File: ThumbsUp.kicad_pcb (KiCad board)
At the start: 2 copper layers, 215.3 x 226 mm, 51 parts, among them J1 52559-1233, J10 Raiser_Male, J13 Raiser_Female, J14 Raiser_Male, J19 Raiser_Female, J1L1 PJ-3200B, J1R1 PJ-3200B, J2 52559-1233, J33 Raiser_Male, J34 Raiser_Female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

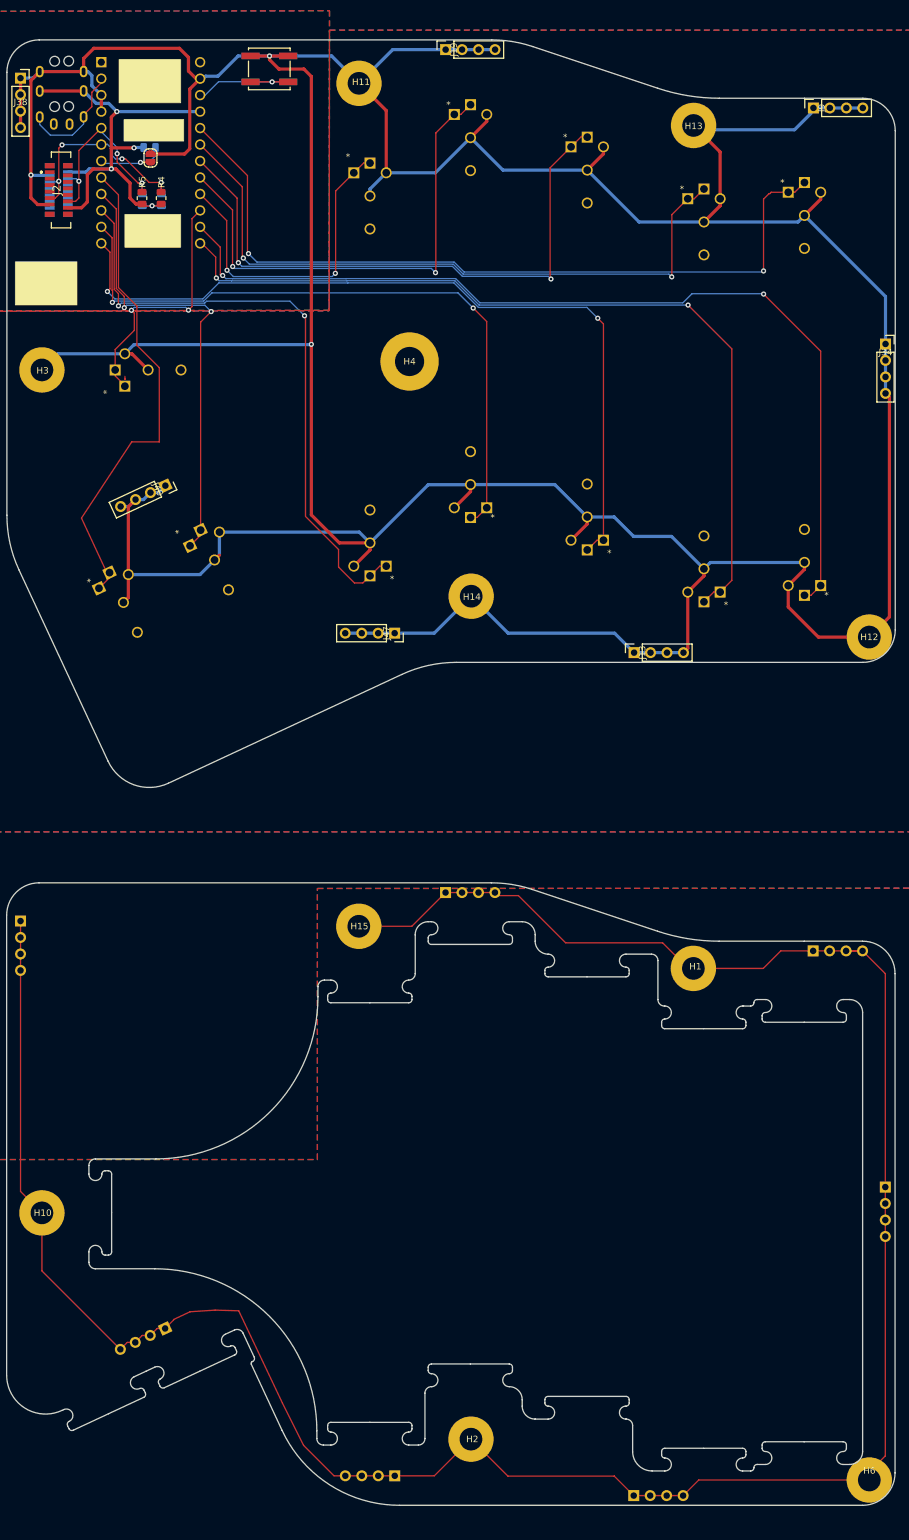
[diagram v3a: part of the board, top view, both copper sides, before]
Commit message: K12: Moved the top border a bit to thicken the bridge between -L and -T. Shuffled the stand-offs and headers around to space them more evenly.//TODO: generate Gerbers
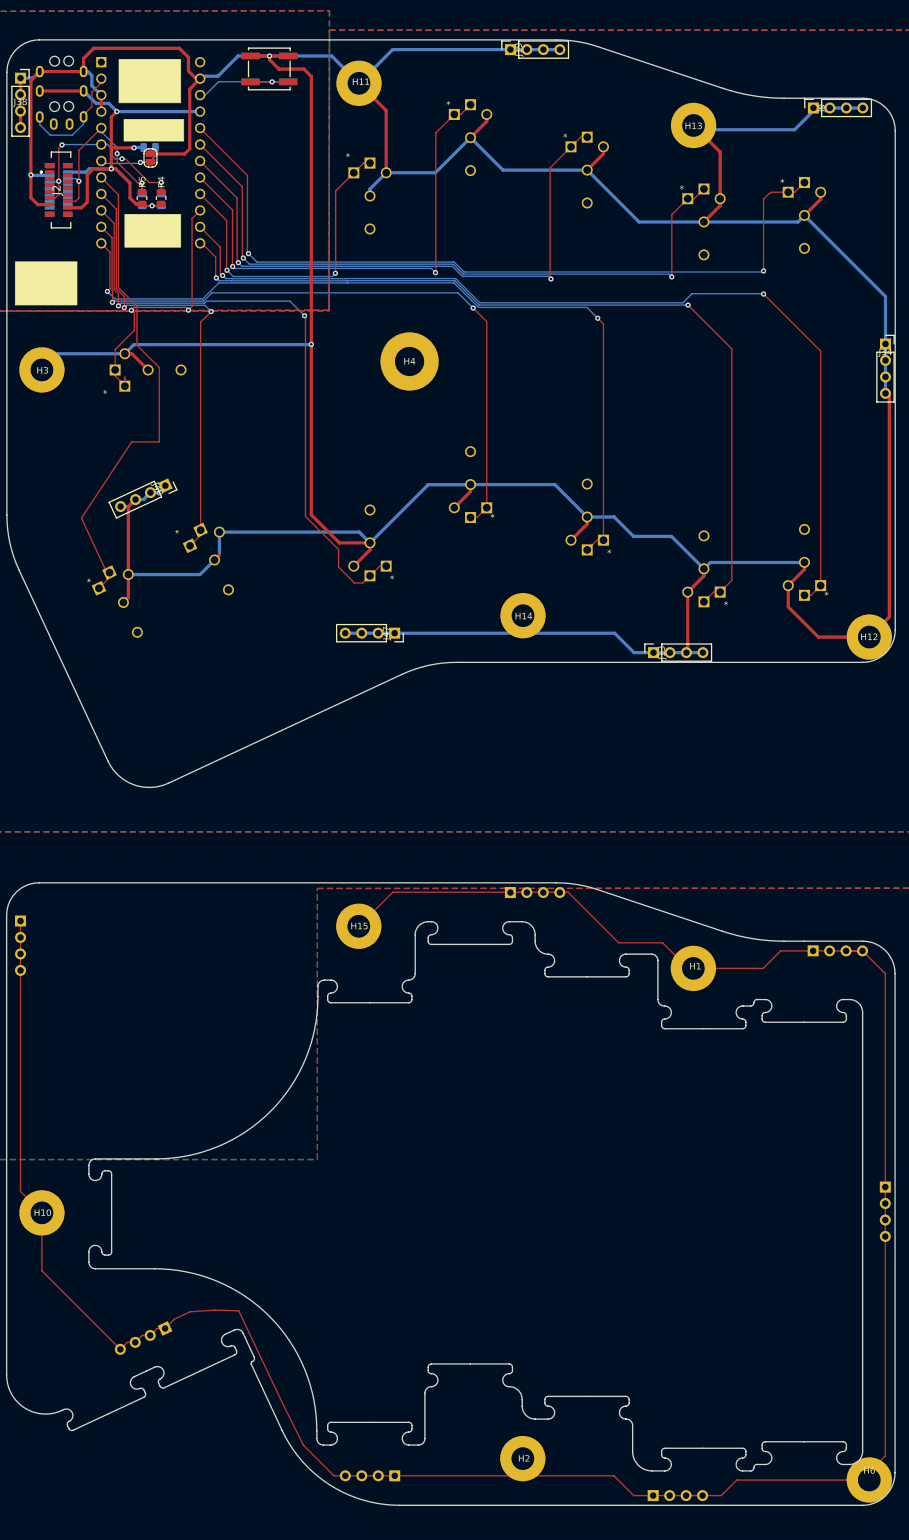
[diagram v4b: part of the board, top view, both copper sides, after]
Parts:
- moved J19 10.0 mm to (109.2, 27.0)
- moved J33 10.0 mm to (109.1, 157.0)
- moved H14 8.54 mm to (111.1, 114.3)
- moved H2 8.54 mm to (111.1, 244.3)
- moved J13 3.00 mm to (131.2, 120.0)
- moved J14 3.00 mm to (131.2, 250.0)
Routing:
- net GND: track 760.9 -> 768.7 mm
- net GNDA: track 384.5 -> 379.9 mm
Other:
- outline, holes or cut-outs redrawn
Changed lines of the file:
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@@
 	(footprint "Connector_PinSocket_2.54mm:PinSocket_1x04_P2.54mm_Vertical"
 		(layer "F.Cu")
-		(at 128.22 120 90)
+		(at 131.22 120 90)
 		(descr "Through hole straight socket strip, 1x04, 2.54mm pitch, single row (from Kicad 4.0.7), script generated")
 		(tags "Through hole socket strip THT 1x04 2.54mm single row")
@@
 	(footprint "Connector_PinSocket_2.54mm:PinSocket_1x04_P2.54mm_Vertical"
 		(layer "F.Cu")
-		(at 99.16 27 90)
+		(at 109.16 27 90)
 		(descr "Through hole straight socket strip, 1x04, 2.54mm pitch, single row (from Kicad 4.0.7), script generated")
 		(tags "Through hole socket strip THT 1x04 2.54mm single row")
@@
 	(footprint "MountingHole:MountingHole_3.5mm_Pad"
 		(layer "F.Cu")
-		(at 103.0683 241.3)
+		(at 111.0683 244.3)
 		(descr "Mounting Hole 3.5mm, generated by kicad-footprint-generator mountinghole.py")
 		(tags "mountinghole")
@@
 	(footprint "MountingHole:MountingHole_3.5mm_Pad"
 		(layer "F.Cu")
-		(at 103.1 111.3)
+		(at 111.1 114.3)
 		(descr "Mounting Hole 3.5mm, generated by kicad-footprint-generator mountinghole.py")
 		(tags "mountinghole")
@@
 	(footprint "Connector_PinHeader_2.54mm:PinHeader_1x04_P2.54mm_Vertical"
 		(layer "B.Cu")
-		(at 128.1683 250 -90)
+		(at 131.1683 250 -90)
 		(descr "Through hole straight pin header, 1x04, 2.54mm pitch, single row")
 		(tags "Through hole pin header THT 1x04 2.54mm single row")
@@
 	(footprint "Connector_PinHeader_2.54mm:PinHeader_1x04_P2.54mm_Vertical"
 		(layer "B.Cu")
-		(at 99.1483 157 -90)
+		(at 109.1483 157 -90)
 		(descr "Through hole straight pin header, 1x04, 2.54mm pitch, single row")
 		(tags "Through hole pin header THT 1x04 2.54mm single row")
@@
 	)
 	(gr_arc
-		(start 106.214447 155.5)
-		(mid 109.418092 155.758251)
-		(end 112.539002 156.526334)
+		(start 116.214447 155.5)
+		(mid 119.418092 155.758251)
+		(end 122.539002 156.526334)
 		(stroke
 			(width 0.05)
@@
 	)
 	(gr_line
-		(start 141.36833 34.5)
+		(start 151.3683 34.5)
 		(end 154.5 34.5)
 		(stroke
@@
 	)
 	(gr_line
-		(start 112.579002 26.526334)
-		(end 131.881497 32.960499)
+		(start 122.579002 26.526334)
+		(end 141.881497 32.960499)
 		(stroke
 			(width 0.05)
@@
 	)
 	(gr_arc
-		(start 106.254447 25.5)
-		(mid 109.458092 25.758251)
-		(end 112.579002 26.526334)
+		(start 116.254447 25.5)
+		(mid 119.458092 25.758251)
+		(end 122.579002 26.526334)
 		(stroke
 			(width 0.05)
@@
 	(gr_line
 		(start 36.5 25.5)
-		(end 106.254447 25.5)
+		(end 116.254447 25.5)
 		(stroke
 			(width 0.05)
@@
 	)
 	(gr_arc
-		(start 141.36833 34.5)
-		(mid 136.562862 34.112628)
-		(end 131.881497 32.960499)
+		(start 151.36833 34.5)
+		(mid 146.562862 34.112628)
+		(end 141.881497 32.960499)
 		(stroke
 			(width 0.05)
@@
 	)
 	(gr_line
-		(start 141.32833 164.5)
+		(start 151.3283 164.5)
 		(end 154.46 164.5)
 		(stroke
@@
 	(gr_line
 		(start 36.46 155.5)
-		(end 106.214447 155.5)
+		(end 116.214447 155.5)
 		(stroke
 			(width 0.05)
@@
 	)
 	(gr_line
-		(start 112.539002 156.526334)
-		(end 131.841497 162.960499)
+		(start 122.539002 156.526334)
+		(end 141.841497 162.960499)
 		(stroke
 			(width 0.05)
@@
 	)
 	(gr_arc
-		(start 141.32833 164.5)
-		(mid 136.522862 164.112628)
-		(end 131.841497 162.960499)
+		(start 151.32833 164.5)
+		(mid 146.522863 164.112625)
+		(end 141.841497 162.960499)
 		(stroke
 			(width 0.05)
@@
 	)
 	(segment
-		(start 107.237524 157.469224)
-		(end 110.389224 157.469224)
-		(width 0.2)
-		(layer "F.Cu")
-		(net 1)
-	)
-	(segment
 		(start 57.2 222.85)
 		(end 57.2 222.928572)
@@
 	)
 	(segment
-		(start 132.62 164.75)
-		(end 136.57 168.7)
+		(start 125.17 247.0017)
+		(end 128.1683 250)
 		(width 0.2)
 		(layer "F.Cu")
@@
 	)
 	(segment
-		(start 51.297978 226.373451)
-		(end 52.371429 225.3)
+		(start 118.05 156.94)
+		(end 125.86 164.75)
 		(width 0.2)
 		(layer "F.Cu")
@@
 	)
 	(segment
-		(start 103.0683 241.3)
-		(end 108.7683 247)
+		(start 51.297978 226.373451)
+		(end 52.371429 225.3)
 		(width 0.2)
 		(layer "F.Cu")
@@
 	)
 	(segment
-		(start 125.17 247)
-		(end 125.17 247.0017)
+		(start 144.07 247.6)
+		(end 164.5 247.6)
 		(width 0.2)
 		(layer "F.Cu")
@@
 	)
 	(segment
-		(start 106.7683 157)
-		(end 107.237524 157.469224)
+		(start 125.86 164.75)
+		(end 132.62 164.75)
 		(width 0.2)
 		(layer "F.Cu")
@@
 	)
 	(segment
-		(start 97.4183 246.95)
-		(end 91.31 246.95)
+		(start 91.0283 156.94)
+		(end 118.05 156.94)
 		(width 0.2)
 		(layer "F.Cu")
@@
 	)
 	(segment
-		(start 108.7683 247)
-		(end 125.17 247)
-		(width 0.2)
-		(layer "F.Cu")
-		(net 1)
-	)
-	(segment
 		(start 85.7683 162.2)
-		(end 93.9483 162.2)
+		(end 91.0283 156.94)
 		(width 0.2)
 		(layer "F.Cu")
@@
 	)
 	(segment
-		(start 93.9483 162.2)
-		(end 99.1483 157)
-		(width 0.2)
-		(layer "F.Cu")
-		(net 1)
-	)
-	(segment
 		(start 33.6 169.01)
 		(end 33.6 203.1)
@@
 	)
 	(segment
-		(start 125.17 247.0017)
-		(end 128.1683 250)
-		(width 0.2)
-		(layer "F.Cu")
-		(net 1)
-	)
-	(segment
 		(start 33.6 161.39)
 		(end 33.6 169.01)
@@
 	)
 	(segment
-		(start 135.7883 250)
-		(end 128.1683 250)
+		(start 91.31 246.95)
+		(end 83.69 246.95)
 		(width 0.2)
 		(layer "F.Cu")
@@
 	(segment
 		(start 91.31 246.95)
-		(end 83.69 246.95)
+		(end 125.17 246.95)
 		(width 0.2)
 		(layer "F.Cu")
@@
 	)
 	(segment
-		(start 164.5 247.6)
-		(end 138.1883 247.6)
+		(start 136.57 168.7)
+		(end 137.3683 168.7)
 		(width 0.2)
 		(layer "F.Cu")
@@
 	)
 	(segment
-		(start 136.57 168.7)
-		(end 137.3683 168.7)
-		(width 0.2)
-		(layer "F.Cu")
-		(net 1)
-	)
-	(segment
-		(start 99.1483 157)
-		(end 106.7683 157)
+		(start 128.1683 250)
+		(end 141.67 250)
 		(width 0.2)
 		(layer "F.Cu")
@@
 	)
 	(segment
-		(start 166.9683 202.42)
-		(end 166.9683 210.04)
+		(start 125.17 246.95)
+		(end 125.17 247.0017)
 		(width 0.2)
 		(layer "F.Cu")
@@
 	)
 	(segment
-		(start 138.1883 247.6)
-		(end 135.7883 250)
+		(start 166.9683 202.42)
+		(end 166.9683 210.04)
 		(width 0.2)
 		(layer "F.Cu")
@@
 	)
 	(segment
-		(start 150.8383 166)
-		(end 163.4583 166)
+		(start 132.62 164.75)
+		(end 136.57 168.7)
 		(width 0.2)
 		(layer "F.Cu")
@@
 	)
 	(segment
-		(start 117.67 164.75)
-		(end 132.62 164.75)
+		(start 150.8383 166)
+		(end 163.4583 166)
 		(width 0.2)
 		(layer "F.Cu")
@@
 	)
 	(segment
-		(start 103.0683 241.3)
-		(end 97.4183 246.95)
+		(start 141.67 250)
+		(end 144.07 247.6)
 		(width 0.2)
 		(layer "F.Cu")
@@
 	)
 	(segment
-		(start 110.389224 157.469224)
-		(end 117.67 164.75)
-		(width 0.2)
-		(layer "F.Cu")
-		(net 1)
-	)
-	(segment
 		(start 72 27.98)
 		(end 72 28.55)
@@
 	)
 	(segment
-		(start 91 27)
-		(end 106.78 27)
-		(width 0.5)
-		(layer "B.Cu")
-		(net 2)
-	)
-	(segment
 		(start 139 107.08)
 		(end 139.98 106.1)
@@
 	)
 	(segment
+		(start 85.8 32.2)
+		(end 91 27)
+		(width 0.5)
+		(layer "B.Cu")
+		(net 2)
+	)
+	(segment
+		(start 91.3 117)
+		(end 125.22 117)
+		(width 0.5)
+		(layer "B.Cu")
+		(net 2)
+	)
+	(segment
 		(start 64.276463 101.410191)
 		(end 85.830191 101.410191)
@@
 	)
 	(segment
-		(start 135.84 120)
-		(end 128.22 120)
-		(width 0.5)
-		(layer "B.Cu")
-		(net 2)
-	)
-	(segment
 		(start 87.5 48.5)
 		(end 90 46)
@@
 	)
 	(segment
-		(start 125.22 117)
-		(end 128.22 120)
+		(start 53.641171 95.319718)
+		(end 54.869743 95.319718)
 		(width 0.5)
 		(layer "B.Cu")
@@
 	)
 	(segment
-		(start 53.641171 95.319718)
-		(end 54.869743 95.319718)
+		(start 128.16 102.08)
+		(end 134 102.08)
 		(width 0.5)
 		(layer "B.Cu")
@@
 	)
 	(segment
-		(start 128.16 102.08)
-		(end 134 102.08)
+		(start 125.22 117)
+		(end 128.22 120)
 		(width 0.5)
 		(layer "B.Cu")
@@
 	)
 	(segment
-		(start 108.8 117)
-		(end 125.22 117)
-		(width 0.5)
-		(layer "B.Cu")
-		(net 2)
-	)
-	(segment
 		(start 167 72.4)
 		(end 167 65.08)
@@
 	)
 	(segment
-		(start 91.3 117)
-		(end 97.4 117)
-		(width 0.5)
-		(layer "B.Cu")
-		(net 2)
-	)
-	(segment
 		(start 50.228692 107.960774)
 		(end 61.274212 107.960774)
@@
 	)
 	(segment
-		(start 156.33 36)
-		(end 158.5 36)
+		(start 136.3 120)
+		(end 138.84 120)
 		(width 0.5)
 		(layer "B.Cu")
@@
 	)
 	(segment
-		(start 85.8 32.2)
-		(end 91 27)
+		(start 156.33 36)
+		(end 158.5 36)
 		(width 0.5)
 		(layer "B.Cu")
@@
 	)
 	(segment
-		(start 103.1 111.3)
-		(end 108.8 117)
-		(width 0.5)
-		(layer "B.Cu")
-		(net 2)
-	)
-	(segment
 		(start 50.265699 97.466619)
 		(end 51.339149 96.393169)
@@
 	)
 	(segment
-		(start 97.4 117)
-		(end 103.1 111.3)
+		(start 128.22 120)
+		(end 135.84 120)
 		(width 0.5)
 		(layer "B.Cu")
@@
 		(width 0.5)
 		(layer "B.Cu")
+		(net 2)
+	)
+	(segment
+		(start 91 27)
+		(end 116.78 27)
+		(width 0.5)
+		(layer "B.Cu")

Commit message: v12: Replaced pin headers/sockets with stand-offs..
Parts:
- removed J10, J14, J33, J35, J39, J41, J48: Raiser_Male, Connector_PinHeader_2.54mm:PinHeader_1x04_P2.54mm_Vertical
- removed J13, J19, J34, J38, J40, J47, J9: Raiser_Female, Connector_PinSocket_2.54mm:PinSocket_1x04_P2.54mm_Vertical
- added H16: MountingHole_Pad, MountingHole:MountingHole_3.5mm_Pad, F.Cu at (87.3, 118.0)
- added H17: MountingHole_Pad, MountingHole:MountingHole_3.5mm_Pad, F.Cu at (35.6, 29.4)
- added H18: MountingHole_Pad, MountingHole:MountingHole_3.5mm_Pad, F.Cu at (49.9, 92.2)
- added H19: MountingHole_Pad, MountingHole:MountingHole_3.5mm_Pad, F.Cu at (167.0, 209.4)
- added H20: MountingHole_Pad, MountingHole:MountingHole_3.5mm_Pad, F.Cu at (139.2, 252.0)
- added H21: MountingHole_Pad, MountingHole:MountingHole_3.5mm_Pad, F.Cu at (87.3, 247.9)
- added H22: MountingHole_Pad, MountingHole:MountingHole_3.5mm_Pad, F.Cu at (35.6, 159.4)
- added H23: MountingHole_Pad, MountingHole:MountingHole_3.5mm_Pad, F.Cu at (49.9, 222.2)
- added H24: MountingHole_Pad, MountingHole:MountingHole_3.5mm_Pad, F.Cu at (114.9, 159.0)
- added H25: MountingHole_Pad, MountingHole:MountingHole_3.5mm_Pad, F.Cu at (166.8, 168.9)
- added H5: MountingHole_Pad, MountingHole:MountingHole_3.5mm_Pad, F.Cu at (115.0, 29.0)
- added H7: MountingHole_Pad, MountingHole:MountingHole_3.5mm_Pad, F.Cu at (166.8, 39.0)
- added H8: MountingHole_Pad, MountingHole:MountingHole_3.5mm_Pad, F.Cu at (167.0, 79.4)
- added H9: MountingHole_Pad, MountingHole:MountingHole_3.5mm_Pad, F.Cu at (139.2, 122.0)
- moved JP1 4.56 mm to (57.6, 46.0)
- moved R17 4.56 mm to (57.4, 44.4), turned to 0 degrees
- moved H12 4.47 mm to (166.5, 121.6)
- moved H6 4.47 mm to (166.5, 251.6)
- moved J1L1 4.00 mm to (45.0, 27.2)
- moved J1R1 4.00 mm to (42.9, 27.2)
- moved R1 4.00 mm to (56.4, 50.2)
- moved R2 4.00 mm to (59.3, 50.2)
- moved R4 4.00 mm to (59.3, 49.9)
- moved R5 4.00 mm to (56.3, 49.9)
- moved STUDIO_UNLOCK1 4.00 mm to (76.0, 30.0)
- moved STUDIO_UNLOCK2 4.00 mm to (76.0, 30.0)
- moved U1 4.00 mm to (57.7, 42.9)
- moved MX26 3.00 mm to (61.4, 98.1)
- moved MX30 3.00 mm to (47.3, 104.7)
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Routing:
- net L-RING1: track 73.4 -> 90.1 mm, vias 4 -> 3
- net GND: track 768.7 -> 785.1 mm, vias 3 -> 16
- net GNDA: track 379.9 -> 389.6 mm
- net RESET: track 20.3 -> 28.8 mm, vias 1 -> 0
- net SwG: track 125.2 -> 118.3 mm
- net SwE: track 75.6 -> 69.4 mm
- net SDA: track 30.5 -> 36.5 mm, vias 3 -> 2
- net SwU: track 70.4 -> 64.8 mm
- net SwZ: track 146.6 -> 141.8 mm
- net SwB: track 104.4 -> 99.8 mm
- net SCL: track 32.4 -> 36.9 mm, vias 4 -> 3
- net SwF: track 50.6 -> 46.8 mm
- net SwT: track 103.7 -> 100.0 mm
- net SwP: track 76.2 -> 72.5 mm
- net SwL: track 92.3 -> 88.6 mm
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- added copper zone on B.Cu, net GND
- added copper zone on F.Cu, net GND
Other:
- board size 215.3 x 226 mm -> 215.3 x 230 mm
